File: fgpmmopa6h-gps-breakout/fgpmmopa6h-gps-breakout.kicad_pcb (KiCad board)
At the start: 2 copper layers, 15 parts, among them J1 BREAKOUT, U1 MIC5365, U2 FGPMMOPA6H-GPS

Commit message: Release FGPMMOPA6H GPS breakout v1.0
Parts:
- BAT1: footprint Wickerlib:BATT-HOLDER-STRAP-CR2032-BC-2003 -> Wickerlib:BATT-HOLDER-CR1220-BK-916
- J1: footprint Wickerlib:CONN-HEADER-STRAIGHT-P2.54MM-1x09 -> Wickerlib:CONN-HEADER-STRAIGHT-P2.54MM-1x10
- moved BAT1 198.2 mm to (175.8, 91.7), turned to 270 degrees
- moved AN1 196.3 mm to (168.4, 100.8)
- moved U2 182.4 mm to (156.0, 94.5)
- moved R3 176.4 mm to (144.0, 101.9), turned to 180 degrees
- moved R1 175.2 mm to (144.0, 99.8)
- moved D1 174.0 mm to (144.1, 97.5)
- moved S1 173.3 mm to (152.0, 83.3), turned to 180 degrees
- moved LED1 172.6 mm to (143.8, 95.5)
- moved R2 171.8 mm to (144.0, 93.7)
- moved C2 170.8 mm to (144.0, 91.9), turned to 180 degrees
- moved C4 168.6 mm to (144.0, 87.6), turned to 180 degrees
- moved C3 167.5 mm to (144.0, 85.6), turned to 180 degrees
- moved U1 165.3 mm to (137.7, 91.4), turned to 270 degrees
- moved C1 163.7 mm to (137.6, 88.6)
- moved J1 154.0 mm to (130.8, 81.3)
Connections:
- net /FTDI_TX renamed /5V_TX
- D1 pad 2: /GPS_RX -> /3.3V_TX
- J1 pad 1: /~FTDI_RESET -> (no net)
- J1 pad 2: /FTDI_RX -> /GPS_RX
- R1 pad 2: /GPS_RX -> /3.3V_TX
- S1 pad 1: /~FTDI_RESET -> /~RESET
- U2 pad 2: /~FTDI_RESET -> /~RESET
- U2 pad 9: /FTDI_RX -> /3.3V_TX
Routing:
- net /VBACKUP: track 0.00 -> 58.5 mm
- net GND: track 0.00 -> 43.7 mm, vias 0 -> 18
- net /1PPS: track 0.00 -> 38.7 mm, vias 0 -> 2
- net /GPS_RX: track 0.00 -> 30.6 mm, vias 0 -> 1
- net /3.3V_TX: track 0.00 -> 29.7 mm
- net +3V3: track 0.00 -> 25.9 mm, vias 0 -> 2
- net /5V_TX: track 0.00 -> 22.8 mm, vias 0 -> 2
- net /GPS_RTCM: track 0.00 -> 22.3 mm, vias 0 -> 2
- net /3D-FIX: track 0.00 -> 19.3 mm
- net /RTCM: track 0.00 -> 12.6 mm
- net +5V: track 0.00 -> 10.9 mm
- net /~RESET: track 0.00 -> 8.37 mm
- net Net-(AN1-PadSIG): track 0.00 -> 3.19 mm
- net Net-(LED1-Pad2): track 0.00 -> 1.87 mm
- added copper zone on B.Cu, net GND
- added copper zone on F.Cu, net GND
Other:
- board outline added: 54.6 x 27.9 mm
- net class Default: clearance 0.254 -> 0.1524
- rule trace_clearance: 0.254 -> 0.1524
- board text added: "1/10/17"
- board text added: "1PPS"
- board text added: "3.3V_TX"
- board text added: "5V"
- board text added: "5V_TX"
- board text added: "FGPMMOPA6H GPS"
- board text added: "FGPMMOPA6H GPS Breakout Board v1.0"
- board text added: "FGPMMOPA6H GPS Breakout Board v1.0 Assembly Diagram"
- board text added: "FIX"
- board text added: "GND"
- board text added: "NC"
- board text added: "RESET"
- board text added: "RTCM"
- board text added: "RX"
- board text added: "wickerbox.net"

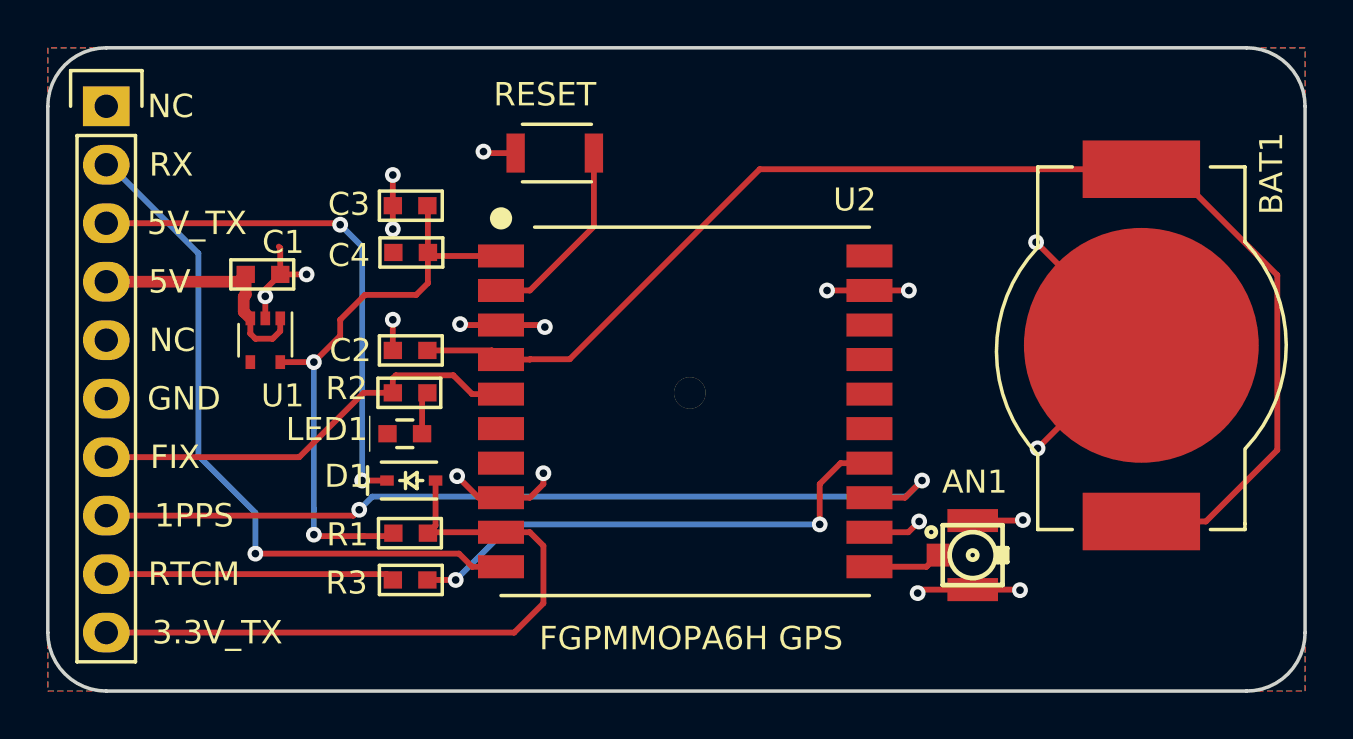
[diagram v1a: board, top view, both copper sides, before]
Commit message: Fixed TX/RX.
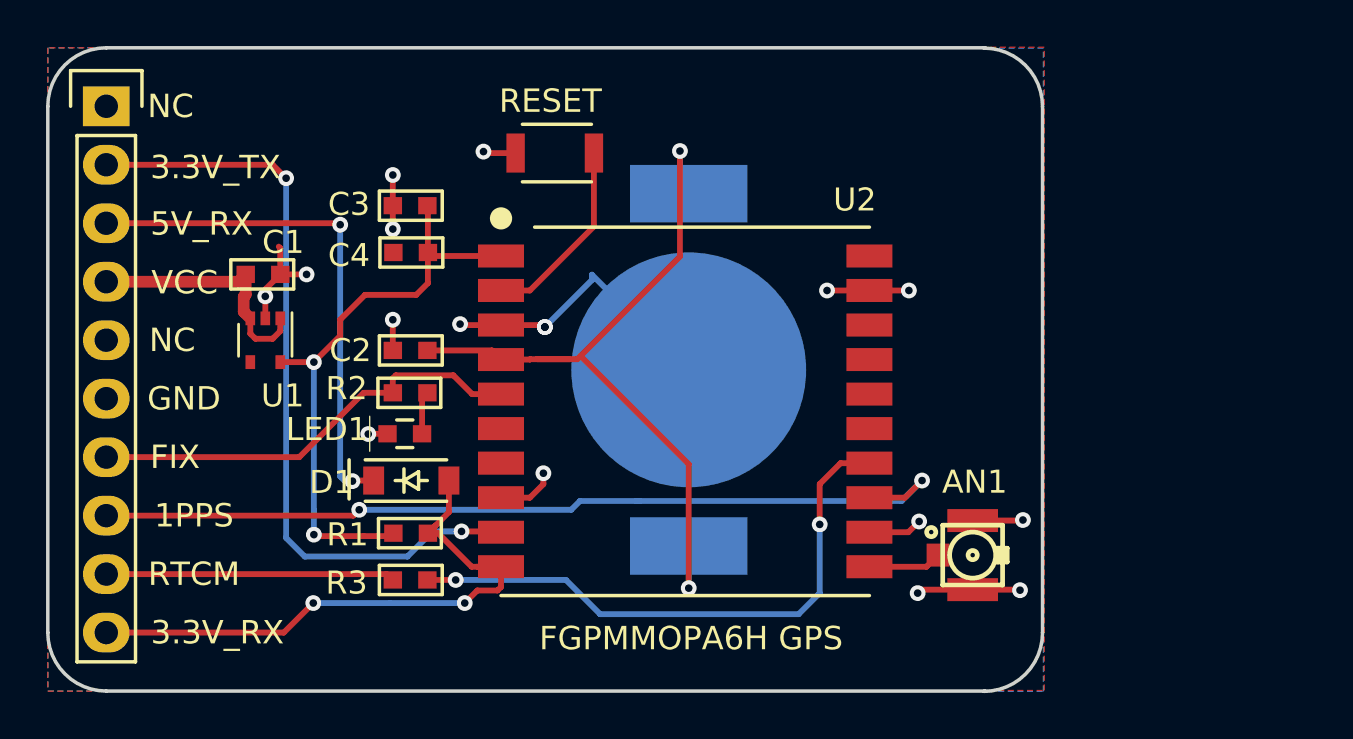
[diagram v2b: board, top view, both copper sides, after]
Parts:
- BAT1: moved to B.Cu
- D1: value BAS16 -> 1N4148; footprint Wickerlib:SOD-323 -> Wickerlib:SOD-123
- moved BAT1 19.7 mm to (156.1, 92.7), turned to 90 degrees
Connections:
- net +5V renamed VCC
- net /5V_TX renamed /5V_RX
- D1 pad 2: /3.3V_TX -> /3.3V_RX
- J1 pad 10: /3.3V_TX -> /3.3V_RX
- J1 pad 2: /GPS_RX -> /3.3V_TX
- R1 pad 2: /3.3V_TX -> /3.3V_RX
- U2 pad 10: /GPS_RX -> /3.3V_RX
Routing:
- net /GPS_RX: track 30.6 -> 0.00 mm, vias 1 -> 0
- net /3.3V_RX: track 0.00 -> 26.2 mm, vias 0 -> 2
- net /VBACKUP: track 58.5 -> 34.9 mm, vias 0 -> 2
- net GND: track 43.7 -> 38.5 mm, vias 18 -> 17
- net /3.3V_TX: track 29.7 -> 34.0 mm, vias 0 -> 2
- net /GPS_RTCM: track 22.3 -> 25.3 mm
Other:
- board size 54.6 x 27.9 mm -> 43.2 x 28 mm
- board text added: "3.3V_RX"
- board text added: "5V_RX"
- board text added: "VCC"
- board text removed: "1/10/17"
- board text removed: "5V"
- board text removed: "5V_TX"
- board text removed: "FGPMMOPA6H GPS Breakout Board v1.0"
- board text removed: "FGPMMOPA6H GPS Breakout Board v1.0 Assembly Diagram"
- board text removed: "RX"

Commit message: Built and verified v1.1.
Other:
- board text added: "FGPMMOPA6H GPS Breakout Board v1.1"
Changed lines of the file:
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@@
     (area 126.8826 78.663799 171.551601 106.768901)
     (thickness 1.6)
-    (drawings 29)
+    (drawings 30)
     (tracks 183)
     (zones 0)
@@
     (pad 20 smd rect (at 8.001 -6.74878) (size 1.99898 1.00076) (layers F.Cu F.Paste F.Mask))
   )
+  (gr_text "FGPMMOPA6H GPS Breakout Board v1.1" (at 154.101801 80.71104) (layer B.SilkS)
+    (effects (font (size 1.016 1.016) (thickness 0.1524)) (justify mirror))
+  )
   (gr_text RESET (at 150.1013 81.0514) (layer F.SilkS)

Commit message: Regenerated bom and gerbers.
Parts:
- moved AN1 135.3 mm to (40.5, 56.7)
- moved BAT1 135.3 mm to (28.2, 48.7)
- moved D1 135.3 mm to (16.1, 53.5)
- moved LED1 135.3 mm to (15.8, 51.5)
- moved S1 135.3 mm to (24.0, 39.3)
- moved U2 135.3 mm to (28.0, 50.5)
- moved C1 135.3 mm to (9.67, 44.6)
- moved C2 135.3 mm to (16.1, 47.9)
- moved C3 135.3 mm to (16.1, 41.6)
- moved C4 135.3 mm to (16.1, 43.6)
- moved J1 135.3 mm to (2.87, 37.3)
- moved R1 135.3 mm to (16.1, 55.8)
- moved R2 135.3 mm to (16.1, 49.7)
- moved R3 135.3 mm to (16.1, 57.8)
- moved U1 135.3 mm to (9.77, 47.4)
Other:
- board text added: "FABRICATION NOTES 1. THIS IS A 2 LAYER BOARD. 2. EXTERNAL LAYERS SHALL HAVE 1 OZ COPPER. 3. MATERIAL: FR4 AND 0.062 INCH +/- 10% THICK. 4. BOARDS SHALL BE ROHS COMPLIANT. 5. MANUFACTURE IN ACCORDANCE WITH IPC-6012 CLASS 2 6. MASK: BOTH SIDES OF THE BOARD SHALL HAVE SOLDER MASK (ANY COLOR) OVER BARE COPPER. 7. SILK: BOTH SIDES OF THE BOARD SHALL HAVE WHITE SILKSCREEN. DO NOT PLACE SILK OVER BARE C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"
